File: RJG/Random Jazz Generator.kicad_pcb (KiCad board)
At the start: 2 copper layers, 167.8 x 200.6 mm, 131 parts, among them J101 EuroPower, J102 CV, J103 RND, J104 Gate, J105 Trig1, J106 Trig2, J107 Clock, J108 Trig3, J109 Trig4, Q101 BC557, Q102 BC547, Q201 BC547, Q202 BC547, Q401 BC547, Q402 BC547, SW101 Reset, SW301 Reload, SW401 Duration Length, SW402 Reload, U101 L7805, U102 4520, U103 TL082, U201 74LS04, U202 74LS595, U301 74HCT4051, U302 74HCT40105, U303 74LS157, U304 74LS157, U401 4520, U402 74LS74, U403 74LS85, U404 74LS157, U405 SST39SF010, U407 74LS173

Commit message: Minor tweaks; added BOM
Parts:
- U102, U401: value 4520 -> 74HCT4520
- U201: value 74LS04 -> 74HCT04
- U202: value 74LS595 -> 74ACHT595
- U303, U304, U404: value 74LS157 -> 74HCT157
- U402: value 74LS74 -> 74HCT74
- U403: value 74LS85 -> 74HCT85
- U406: renamed from U407; value 74LS173 -> 74HCT173
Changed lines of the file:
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@@
       (effects (font (size 1 1) (thickness 0.15)) (justify mirror))
     )
-    (fp_text value 74LS157 (at 4.52 19 180) (layer B.SilkS)
+    (fp_text value 74HCT157 (at 5.12 14.8 270) (layer B.SilkS)
       (effects (font (size 1 1) (thickness 0.15)) (justify mirror))
     )
@@
       (effects (font (size 1 1) (thickness 0.15)) (justify mirror))
     )
-    (fp_text value 74LS157 (at 4.6 18.9) (layer B.SilkS)
+    (fp_text value 74HCT157 (at 5.4 14.8 90) (layer B.SilkS)
       (effects (font (size 1 1) (thickness 0.15)) (justify mirror))
     )
@@
     (descr "16-lead though-hole mounted DIP package, row spacing 7.62 mm (300 mils), LongPads")
     (tags "THT DIP DIL PDIP 2.54mm 7.62mm 300mil LongPads")
-    (fp_text reference U407 (at 3.9 17.76) (layer B.SilkS)
-      (effects (font (size 1 1) (thickness 0.15)) (justify mirror))
-    )
-    (fp_text value 74LS173 (at 2.9 2.46 90) (layer B.SilkS)
+    (fp_text reference U406 (at 3.9 17.76) (layer B.SilkS)
+      (effects (font (size 1 1) (thickness 0.15)) (justify mirror))
+    )
+    (fp_text value 74HCT173 (at 2.4 2.76 90) (layer B.SilkS)
       (effects (font (size 1 1) (thickness 0.15)) (justify mirror))
     )
@@
       (effects (font (size 1 1) (thickness 0.15)) (justify mirror))
     )
-    (fp_text value 74LS157 (at 3.81 20.11) (layer B.SilkS)
+    (fp_text value 74HCT157 (at 3.81 20.11) (layer B.SilkS)
       (effects (font (size 1 1) (thickness 0.15)) (justify mirror))
     )
@@
       (effects (font (size 1 1) (thickness 0.15)) (justify mirror))
     )
-    (fp_text value 74LS85 (at 3.9 1.3) (layer B.SilkS)
+    (fp_text value 74HCT85 (at 2.3 2.5 90) (layer B.SilkS)
       (effects (font (size 1 1) (thickness 0.15)) (justify mirror))
     )
@@
       (effects (font (size 1 1) (thickness 0.15)) (justify mirror))
     )
-    (fp_text value 74LS74 (at 3.72 17) (layer B.SilkS)
+    (fp_text value 74HCT74 (at 3.72 17) (layer B.SilkS)
       (effects (font (size 1 1) (thickness 0.15)) (justify mirror))
     )
@@
       (effects (font (size 1 1) (thickness 0.15)) (justify mirror))
     )
-    (fp_text value 4520 (at 3.9 17.78) (layer B.SilkS)
+    (fp_text value 74HCT4520 (at 5.4 14.58 90) (layer B.SilkS)
       (effects (font (size 1 1) (thickness 0.15)) (justify mirror))
     )
@@
       (effects (font (size 1 1) (thickness 0.15)) (justify mirror))
     )
-    (fp_text value 74LS595 (at 3.81 20.11) (layer B.SilkS)
+    (fp_text value 74ACHT595 (at 3.81 20.11) (layer B.SilkS)
       (effects (font (size 1 1) (thickness 0.15)) (justify mirror))
     )
@@
       (effects (font (size 1 1) (thickness 0.15)) (justify mirror))
     )
-    (fp_text value 74LS04 (at 3.484698 16.53) (layer B.SilkS)
+    (fp_text value 74HCT04 (at 3.484698 16.53) (layer B.SilkS)
       (effects (font (size 1 1) (thickness 0.15)) (justify mirror))
     )
@@
       (effects (font (size 1 1) (thickness 0.15)) (justify mirror))
     )
-    (fp_text value 4520 (at 3.9 -0.06) (layer B.SilkS)
-      (effects (font (size 1 1) (thickness 0.15)) (justify mirror))
-    )
+    (fp_text value 74HCT4520 (at 2.3 3.34 90) (layer B.SilkS)
+      (effects (font (size 1 1) (thickness 0.15)) (justify mirror))
+    )

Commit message: Look! I made a stickman!
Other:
- board text added: "Original idea from R0d0t!"
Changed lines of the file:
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@@
   (general
     (thickness 1.6)
-    (drawings 339)
+    (drawings 343)
     (tracks 839)
     (zones 0)
@@
   (page A4 portrait)
   (layers
-    (0 F.Cu signal hide)
-    (31 B.Cu signal hide)
-    (32 B.Adhes user hide)
-    (33 F.Adhes user hide)
-    (34 B.Paste user hide)
-    (35 F.Paste user hide)
+    (0 F.Cu signal)
+    (31 B.Cu signal)
+    (32 B.Adhes user)
+    (33 F.Adhes user)
+    (34 B.Paste user)
+    (35 F.Paste user)
     (36 B.SilkS user)
-    (37 F.SilkS user hide)
+    (37 F.SilkS user)
     (38 B.Mask user)
-    (39 F.Mask user hide)
-    (40 Dwgs.User user hide)
-    (41 Cmts.User user hide)
-    (42 Eco1.User user hide)
-    (43 Eco2.User user hide)
+    (39 F.Mask user)
+    (40 Dwgs.User user)
+    (41 Cmts.User user)
+    (42 Eco1.User user)
+    (43 Eco2.User user)
     (44 Edge.Cuts user)
-    (45 Margin user hide)
-    (46 B.CrtYd user hide)
-    (47 F.CrtYd user hide)
+    (45 Margin user)
+    (46 B.CrtYd user)
+    (47 F.CrtYd user)
     (48 B.Fab user)
-    (49 F.Fab user hide)
+    (49 F.Fab user)
   )
   (setup
@@
     )
   )
+  (gr_line (start 143.5 147.8) (end 148 150.7) (layer F.SilkS) (width 0.25))
+  (gr_line (start 148.6 158.2) (end 152.8 159.4) (layer F.SilkS) (width 0.25))
+  (gr_line (start 148 150.7) (end 148.6 158.2) (layer F.SilkS) (width 0.25))
+  (gr_text "Original idea from R0d0t!" (at 151.7 209.2) (layer B.SilkS)
+    (effects (font (size 2 2) (thickness 0.25)) (justify mirror))
+  )
   (gr_text +12V (at 34.1 24.5 45) (layer F.SilkS)

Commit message: RJG done !
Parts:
- added D106: 1N4148, Diode_THT:D_DO-35_SOD27_P7.62mm_Horizontal, F.Cu at (157.3, 165.2)
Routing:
- net Net-(D106-Pad1): track 6.86 -> 14.7 mm

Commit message: Added PCB ref stamp and send to prod!
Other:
- board text added: "PCB ref here:"
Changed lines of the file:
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@@
   (general
     (thickness 1.6)
-    (drawings 343)
+    (drawings 348)
     (tracks 841)
     (zones 0)
@@
     (35 F.Paste user)
     (36 B.SilkS user)
-    (37 F.SilkS user hide)
+    (37 F.SilkS user)
     (38 B.Mask user)
     (39 F.Mask user)
@@
   )
   (setup
-    (last_trace_width 0.762)
+    (last_trace_width 0.1524)
     (user_trace_width 0.1524)
     (user_trace_width 0.254)
@@
     )
   )
+  (gr_text "PCB ref here:" (at 166.5 14.3) (layer B.SilkS)
+    (effects (font (size 1 1) (thickness 0.15)) (justify mirror))
+  )
+  (gr_line (start 156.5 13.4) (end 156.5 17.7) (layer B.SilkS) (width 0.15))
+  (gr_line (start 172.3 13.4) (end 156.5 13.4) (layer B.SilkS) (width 0.15))
+  (gr_line (start 172.3 17.7) (end 172.3 13.4) (layer B.SilkS) (width 0.15))
+  (gr_line (start 156.5 17.7) (end 172.3 17.7) (layer B.SilkS) (width 0.15))
   (gr_line (start 143.5 147.8) (end 148 150.7) (layer F.SilkS) (width 0.25))
   (gr_line (start 148.6 158.2) (end 152.8 159.4) (layer F.SilkS) (width 0.25))
@@
   (segment (start 148.9 170) (end 148.7 167.4) (width 0.762) (layer F.Cu) (net 61))
   (segment (start 148.7 167.4) (end 148.9 164.840819) (width 0.762) (layer F.Cu) (net 61))
-  (segment (start 148.4 173.04) (end 151.44 170) (width 0.762) (layer F.Cu) (net 160))
-  (segment (start 148.4 175.6) (end 148.4 173.04) (width 0.762) (layer F.Cu) (net 160))
   (segment (start 21.44 136.62) (end 21.36 136.7) (width 1.016) (layer B.Cu) (net 63))
   (segment (start 21.44 129.5) (end 21.44 136.62) (width 1.016) (layer B.Cu) (net 63))
@@
   (segment (start 15.2 151.55) (end 15.2 153.6) (width 0.762) (layer B.Cu) (net 158))
   (segment (start 15.2 168) (end 15.2 170.05) (width 0.762) (layer B.Cu) (net 159))
+  (segment (start 148.4 173.04) (end 151.44 170) (width 0.762) (layer F.Cu) (net 160))
+  (segment (start 148.4 175.6) (end 148.4 173.04) (width 0.762) (layer F.Cu) (net 160))
   (segment (start 156.24 165.2) (end 157.3 165.2) (width 0.762) (layer F.Cu) (net 160))
   (segment (start 151.44 170) (end 156.24 165.2) (width 0.762) (layer F.Cu) (net 160))

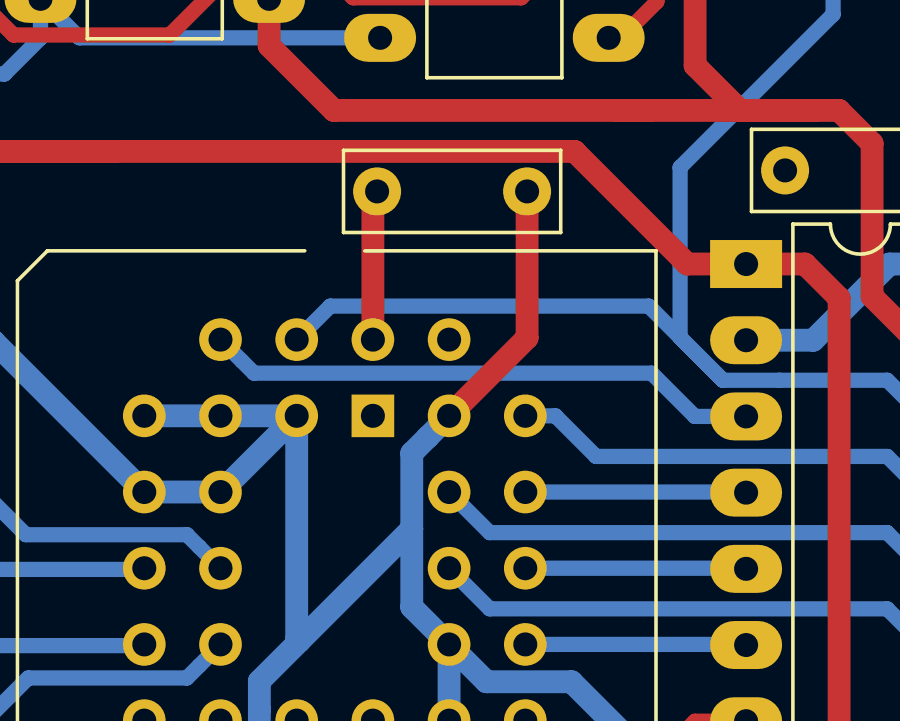
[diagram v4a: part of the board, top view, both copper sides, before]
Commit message: fix badly connected pin
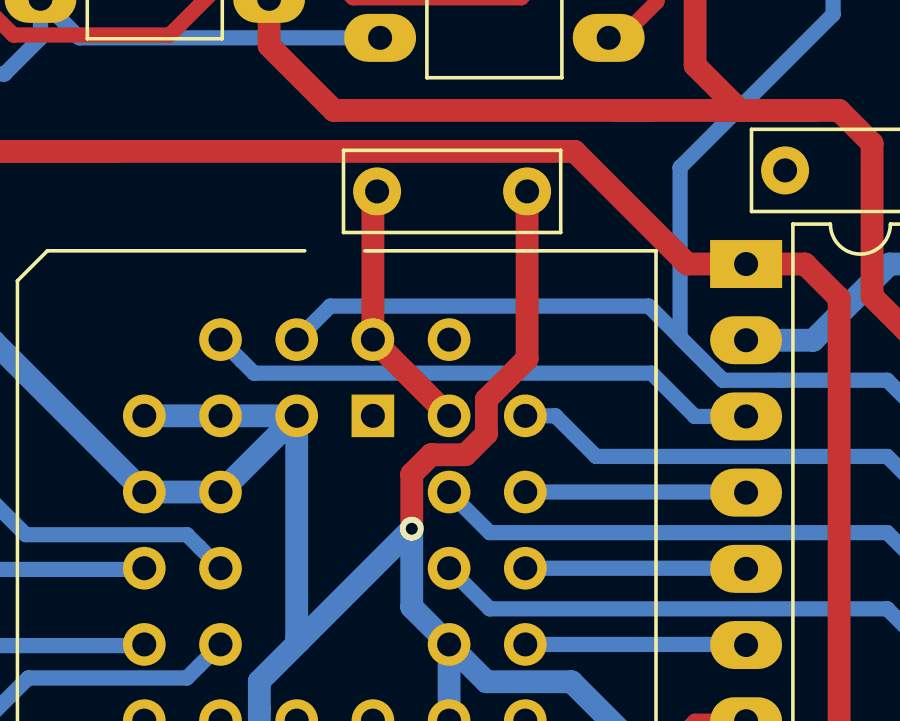
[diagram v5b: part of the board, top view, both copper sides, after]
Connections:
- U405 pad 31: GND -> +5V
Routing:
- net +5V: track 97.4 -> 101.0 mm
- net GND: track 161.6 -> 162.3 mm, vias 0 -> 1
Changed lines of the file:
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@@
     (thickness 1.6)
     (drawings 348)
-    (tracks 841)
+    (tracks 846)
     (zones 0)
     (modules 132)
@@
   )
   (setup
-    (last_trace_width 0.1524)
+    (last_trace_width 0.762)
     (user_trace_width 0.1524)
     (user_trace_width 0.254)
@@
       (net 144 "Net-(U405-Pad11)"))
     (pad 31 thru_hole circle (at 2.54 0) (size 1.4224 1.4224) (drill 0.8) (layers *.Cu *.Mask)
-      (net 1 GND))
+      (net 3 +5V))
     (pad 19 thru_hole circle (at 0 10.16) (size 1.4224 1.4224) (drill 0.8) (layers *.Cu *.Mask)
       (net 126 "Net-(U404-Pad5)"))
@@
   (segment (start 97.772 116.034526) (end 97.772 118.132) (width 0.508) (layer F.Cu) (net 1))
   (segment (start 81.4 144.74) (end 81.4 142.2) (width 0.762) (layer B.Cu) (net 1))
-  (segment (start 80.688801 135.291199) (end 81.4 134.58) (width 0.762) (layer B.Cu) (net 1))
-  (segment (start 80.155399 135.824601) (end 80.688801 135.291199) (width 0.762) (layer B.Cu) (net 1))
   (segment (start 81.4 142.2) (end 80.155399 140.955399) (width 0.762) (layer B.Cu) (net 1))
   (segment (start 75.608801 146.568801) (end 76.32 147.28) (width 0.762) (layer B.Cu) (net 1))
   (segment (start 80.155399 140.955399) (end 80.155399 138.344601) (width 0.762) (layer B.Cu) (net 1))
   (segment (start 75.075399 146.035399) (end 75.608801 146.568801) (width 0.762) (layer B.Cu) (net 1))
-  (segment (start 80.155399 138.344601) (end 80.155399 135.824601) (width 0.762) (layer B.Cu) (net 1))
   (segment (start 71.24 134.58) (end 76.32 134.58) (width 0.762) (layer B.Cu) (net 1))
   (segment (start 71.24 137.12) (end 73.78 137.12) (width 0.762) (layer B.Cu) (net 1))
@@
   (segment (start 99.94 154.14) (end 102.1 156.3) (width 0.762) (layer F.Cu) (net 1))
   (segment (start 98.92 154.14) (end 99.94 154.14) (width 0.762) (layer F.Cu) (net 1))
-  (segment (start 84 131.98) (end 84 127.1) (width 0.762) (layer F.Cu) (net 1))
-  (segment (start 81.4 134.58) (end 84 131.98) (width 0.762) (layer F.Cu) (net 1))
   (segment (start 33.3 185.175) (end 33.27 185.205) (width 1.016) (layer B.Cu) (net 1))
   (segment (start 33.3 183.1) (end 33.3 185.175) (width 1.016) (layer B.Cu) (net 1))
@@
   (segment (start 100.16 63.84) (end 100.16 66.48) (width 0.508) (layer B.Cu) (net 1))
   (segment (start 102.8 61.2) (end 100.16 63.84) (width 0.508) (layer B.Cu) (net 1))
+  (segment (start 84 132.67799) (end 82.644601 134.033389) (width 0.762) (layer F.Cu) (net 1))
+  (segment (start 84 127.1) (end 84 132.67799) (width 0.762) (layer F.Cu) (net 1))
+  (segment (start 80.802591 135.875399) (end 80.155399 136.522591) (width 0.762) (layer F.Cu) (net 1))
+  (segment (start 82.644601 134.033389) (end 82.644601 135.177409) (width 0.762) (layer F.Cu) (net 1))
+  (segment (start 82.644601 135.177409) (end 81.946611 135.875399) (width 0.762) (layer F.Cu) (net 1))
+  (segment (start 81.946611 135.875399) (end 80.802591 135.875399) (width 0.762) (layer F.Cu) (net 1))
+  (segment (start 80.155399 136.522591) (end 80.155399 138.344601) (width 0.762) (layer F.Cu) (net 1))
+  (segment (start 80.155399 138.344601) (end 80.155399 138.344601) (width 0.762) (layer F.Cu) (net 1))
+  (via (at 80.155399 138.344601) (size 0.8) (drill 0.4) (layers F.Cu B.Cu) (net 1))
   (segment (start 35.3 30.54) (end 35.3 28) (width 1.016) (layer B.Cu) (net 2))
   (segment (start 15.139599 63.223007) (end 15.139599 135.639599) (width 1.016) (layer B.Cu) (net 2))
@@
   (segment (start 93.460001 103.500001) (end 94.16 104.2) (width 0.762) (layer B.Cu) (net 3))
   (segment (start 88.682 104.2) (end 89.715401 103.166599) (width 0.762) (layer B.Cu) (net 3))
+  (segment (start 78.86 132.04) (end 81.4 134.58) (width 0.762) (layer F.Cu) (net 3))
   (segment (start 89.6 109.14) (end 91.8 106.94) (width 0.762) (layer F.Cu) (net 4))
   (segment (start 89.6 122.9) (end 89.6 109.14) (width 0.762) (layer F.Cu) (net 4))

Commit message: fix stuffs
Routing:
- net +5V: vias 11 -> 12
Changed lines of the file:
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@@
     (thickness 1.6)
     (drawings 348)
-    (tracks 846)
+    (tracks 848)
     (zones 0)
     (modules 132)
@@
   )
   (setup
-    (last_trace_width 0.762)
+    (last_trace_width 0.1524)
     (user_trace_width 0.1524)
     (user_trace_width 0.254)
@@
   (segment (start 84.8 91.2) (end 86.7 91.2) (width 0.762) (layer B.Cu) (net 3))
   (segment (start 93.126599 103.166599) (end 93.460001 103.500001) (width 0.762) (layer B.Cu) (net 3))
-  (segment (start 89.715401 103.166599) (end 93.126599 103.166599) (width 0.762) (layer B.Cu) (net 3))
+  (segment (start 89.715401 103.166599) (end 90.233401 103.166599) (width 0.762) (layer B.Cu) (net 3))
   (segment (start 86.72 104.2) (end 88.682 104.2) (width 0.762) (layer B.Cu) (net 3))
   (segment (start 93.460001 103.500001) (end 94.16 104.2) (width 0.762) (layer B.Cu) (net 3))
   (segment (start 88.682 104.2) (end 89.715401 103.166599) (width 0.762) (layer B.Cu) (net 3))
   (segment (start 78.86 132.04) (end 81.4 134.58) (width 0.762) (layer F.Cu) (net 3))
+  (segment (start 90.233401 103.166599) (end 93.126599 103.166599) (width 0.762) (layer B.Cu) (net 3))
+  (via (at 90.233401 103.166599) (size 0.8) (drill 0.4) (layers F.Cu B.Cu) (net 3))
   (segment (start 89.6 109.14) (end 91.8 106.94) (width 0.762) (layer F.Cu) (net 4))
   (segment (start 89.6 122.9) (end 89.6 109.14) (width 0.762) (layer F.Cu) (net 4))
@@
       )
     )
+  )
+  (zone (net 0) (net_name "") (layers F&B.Cu) (hatch edge 0.508)
+    (connect_pads (clearance 0.508))
+    (min_thickness 0.254)
+    (keepout (tracks allowed) (vias allowed) (copperpour not_allowed))
+    (fill (arc_segments 32) (thermal_gap 0.508) (thermal_bridge_width 0.508))
+    (polygon
+      (pts
+        (xy 108.9 120.8) (xy 105.2 120.8) (xy 105.2 105.4) (xy 108.9 105.4)
+      )
+    )
